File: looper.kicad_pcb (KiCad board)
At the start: 2 copper layers, 83 x 56.2 mm, 93 parts, among them CON1 BARREL_JACK, J1 JMP, J2 UART, J3 programming header, J4 Micro_SD_Card_Det, J5 electret mic, J6 line in, J7 line/~mic, J8 stereo_out, SW1 reset, SW2 RAM~FLASH, SW3 start, SW4 stop, SW5 Rotary_Encoder_Switch, U1 WM8778-units, U2 AP3211, U3 AZ1117C, U4 TC1185, U5 STM32F401RC, U6 lcd, U7 MAX4466, Y1 CSTLS4M00G53-B0

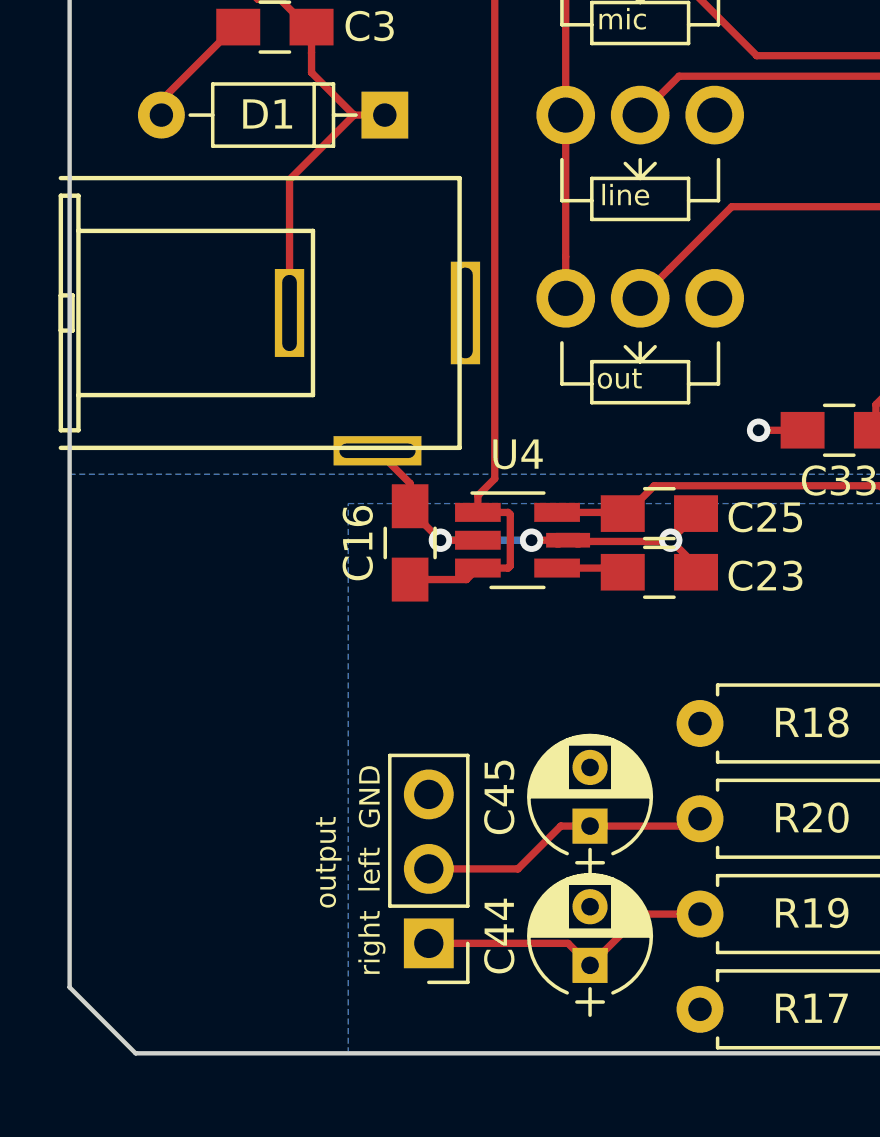
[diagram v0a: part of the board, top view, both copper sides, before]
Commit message: k: fix pcb
power connector trouble
wrong footprint for caps
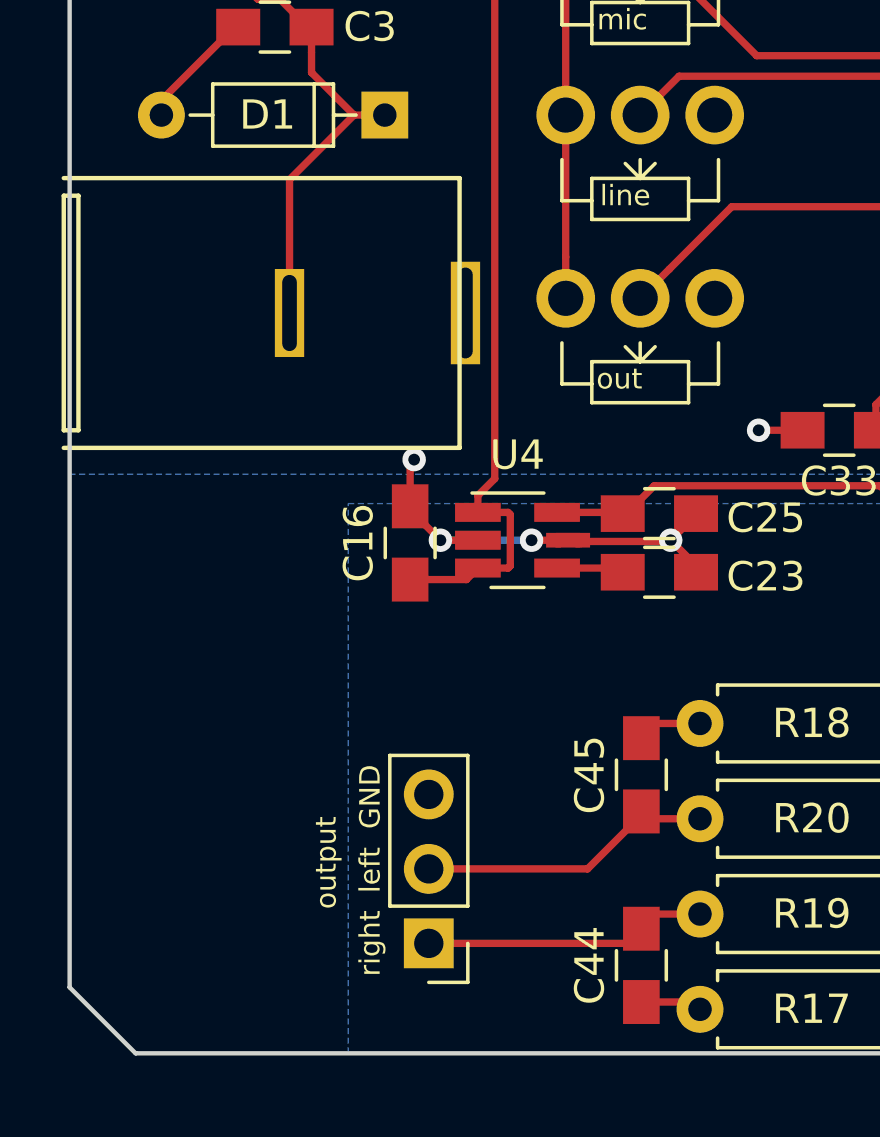
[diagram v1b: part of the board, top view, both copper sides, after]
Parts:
- C44, C45: footprint Capacitors_THT:CP_Radial_D4.0mm_P2.00mm -> Capacitors_SMD:C_0805_HandSoldering
- moved C45 2.47 mm to (68.8, 77.5)
- moved C44 1.75 mm to (68.8, 84.0), turned to 270 degrees
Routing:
- net AGND: track 21.7 -> 26.0 mm
- net GND: track 73.0 -> 72.3 mm, vias 25 -> 26
- net /Codec/voutl: track 9.96 -> 10.6 mm
- net /Codec/voutr: track 10.3 -> 9.66 mm

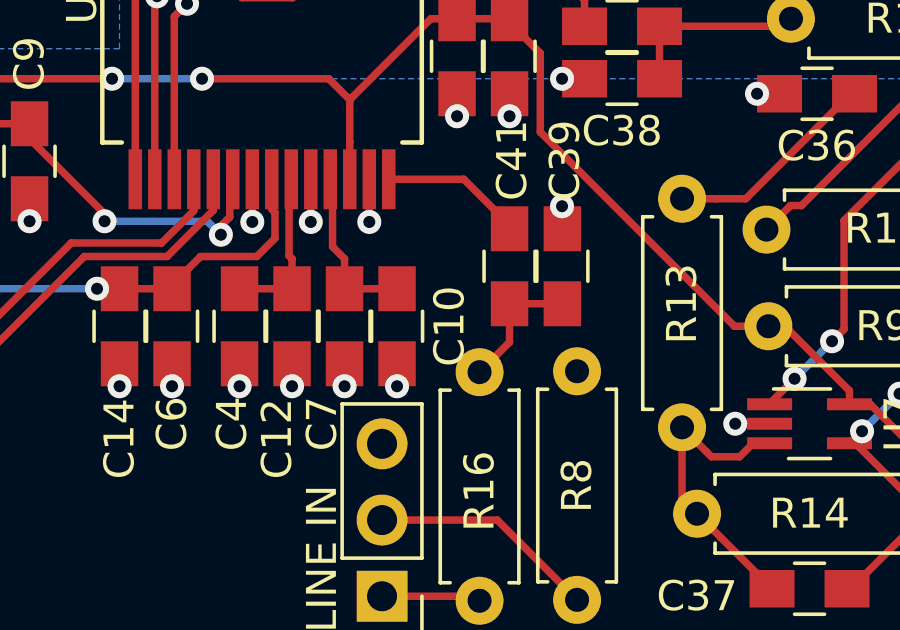
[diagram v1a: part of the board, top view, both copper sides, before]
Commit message: ksch: change component values to include the unit except for resistors add more info to some devices
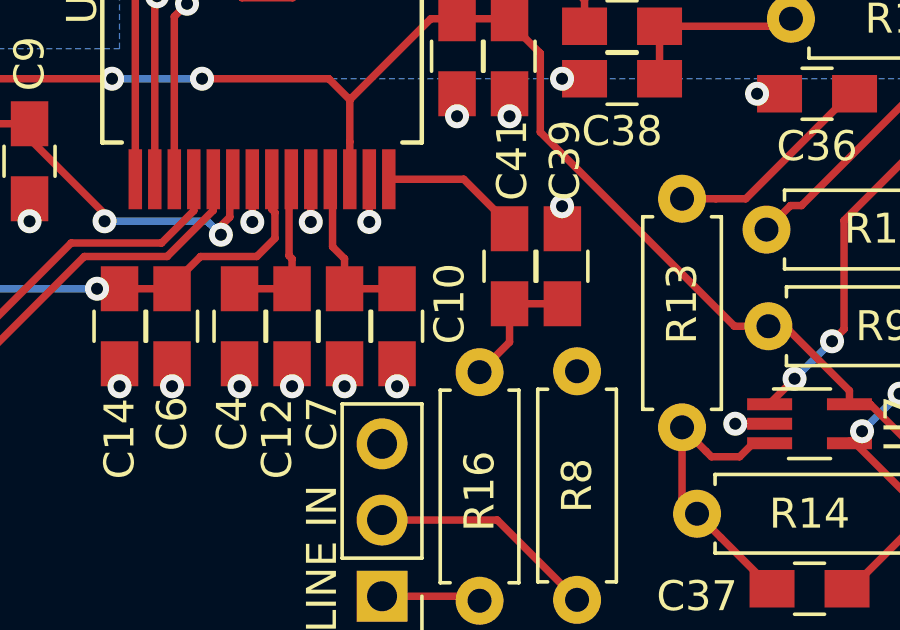
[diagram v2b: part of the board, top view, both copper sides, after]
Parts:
- C17, C33, C34: value 0.1u -> 100nF
- C19, C21, C26, C27, C28, C29: value 100n -> 100nF
- C2, C4, C5, C6, C7, C9: value 0.1uF -> 100nF
- C20, C36: value 1u -> 1uF
- C22, C30, C31: value 4.7u -> 4.7uF
- C32, C40, C41: value 10u -> 10uF
- C35: value 0.01u -> 10nF
- C37: value 100p -> 100pF
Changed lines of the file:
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@@
       (effects (font (size 1 1) (thickness 0.15)))
     )
-    (fp_text value 4.7u (at 0 1.75 270) (layer F.Fab)
+    (fp_text value 4.7uF (at 0 1.75 270) (layer F.Fab)
       (effects (font (size 1 1) (thickness 0.15)))
     )
@@
       (effects (font (size 1 1) (thickness 0.15)))
     )
-    (fp_text value 0.1u (at 0 1.75 90) (layer F.Fab)
+    (fp_text value 100nF (at 0 1.75 90) (layer F.Fab)
       (effects (font (size 1 1) (thickness 0.15)))
     )
@@
       (effects (font (size 1 1) (thickness 0.15)))
     )
-    (fp_text value 100n (at 0 1.75) (layer F.Fab)
+    (fp_text value 100nF (at 0 1.75) (layer F.Fab)
       (effects (font (size 1 1) (thickness 0.15)))
     )
@@
       (effects (font (size 1 1) (thickness 0.15)))
     )
-    (fp_text value 100n (at 0 1.75 90) (layer F.Fab)
+    (fp_text value 100nF (at 0 1.75 90) (layer F.Fab)
       (effects (font (size 1 1) (thickness 0.15)))
     )
@@
       (effects (font (size 1 1) (thickness 0.15)))
     )
-    (fp_text value 100n (at 0 1.75 180) (layer F.Fab)
+    (fp_text value 100nF (at 0 1.75 180) (layer F.Fab)
       (effects (font (size 1 1) (thickness 0.15)))
     )
@@
       (effects (font (size 1 1) (thickness 0.15)))
     )
-    (fp_text value 100n (at 0 1.75 270) (layer F.Fab)
+    (fp_text value 100nF (at 0 1.75 270) (layer F.Fab)
       (effects (font (size 1 1) (thickness 0.15)))
     )
@@
       (effects (font (size 1 1) (thickness 0.15)))
     )
-    (fp_text value 100n (at 0 1.75 270) (layer F.Fab)
+    (fp_text value 100nF (at 0 1.75 270) (layer F.Fab)
       (effects (font (size 1 1) (thickness 0.15)))
     )
@@
       (effects (font (size 1 1) (thickness 0.15)))
     )
-    (fp_text value 100n (at 0 1.75 90) (layer F.Fab)
+    (fp_text value 100nF (at 0 1.75 90) (layer F.Fab)
       (effects (font (size 1 1) (thickness 0.15)))
     )
@@
       (effects (font (size 1 1) (thickness 0.15)))
     )
-    (fp_text value 4.7u (at 0 1.75 90) (layer F.Fab)
+    (fp_text value 4.7uF (at 0 1.75 90) (layer F.Fab)
       (effects (font (size 1 1) (thickness 0.15)))
     )
@@
       (effects (font (size 1 1) (thickness 0.15)))
     )
-    (fp_text value 4.7u (at 0 1.75 90) (layer F.Fab)
+    (fp_text value 4.7uF (at 0 1.75 90) (layer F.Fab)
       (effects (font (size 1 1) (thickness 0.15)))
     )
@@
       (effects (font (size 1 1) (thickness 0.15)))
     )
-    (fp_text value 10u (at 0 1.75 90) (layer F.Fab)
+    (fp_text value 10uF (at 0 1.75 90) (layer F.Fab)
       (effects (font (size 1 1) (thickness 0.15)))
     )
@@
       (effects (font (size 1 1) (thickness 0.15)))
     )
-    (fp_text value 0.1u (at 0 1.75 180) (layer F.Fab)
+    (fp_text value 100nF (at 0 1.75 180) (layer F.Fab)
       (effects (font (size 1 1) (thickness 0.15)))
     )
@@
       (effects (font (size 1 1) (thickness 0.15)))
     )
-    (fp_text value 0.1u (at 0 1.75 90) (layer F.Fab)
+    (fp_text value 100nF (at 0 1.75 90) (layer F.Fab)
       (effects (font (size 1 1) (thickness 0.15)))
     )
@@
       (effects (font (size 1 1) (thickness 0.15)))
     )
-    (fp_text value 0.01u (at 0 1.75) (layer F.Fab)
+    (fp_text value 10nF (at 0 1.75) (layer F.Fab)
       (effects (font (size 1 1) (thickness 0.15)))
     )
@@
       (effects (font (size 1 1) (thickness 0.15)))
     )
-    (fp_text value 1u (at 0 1.75 180) (layer F.Fab)
+    (fp_text value 1uF (at 0 1.75 180) (layer F.Fab)
       (effects (font (size 1 1) (thickness 0.15)))
     )
@@
       (effects (font (size 1 1) (thickness 0.15)))
     )
-    (fp_text value 100p (at 0 1.75 180) (layer F.Fab)
+    (fp_text value 100pF (at 0 1.75 180) (layer F.Fab)
       (effects (font (size 1 1) (thickness 0.15)))
     )
@@
       (effects (font (size 1 1) (thickness 0.15)))
     )
-    (fp_text value 10u (at 0 0) (layer F.Fab)
+    (fp_text value 10uF (at 0 0) (layer F.Fab)
       (effects (font (size 1 1) (thickness 0.15)))
     )
@@
       (effects (font (size 1 1) (thickness 0.15)))
     )
-    (fp_text value 1u (at 0 0 90) (layer F.Fab)
+    (fp_text value 1uF (at 0 0 90) (layer F.Fab)
       (effects (font (size 1 1) (thickness 0.15)))
     )
@@
       (effects (font (size 1 1) (thickness 0.15)))
     )
-    (fp_text value 10u (at 0 1.75 270) (layer F.Fab)
+    (fp_text value 10uF (at 0 1.75 270) (layer F.Fab)
       (effects (font (size 1 1) (thickness 0.15)))
     )
@@
       (effects (font (size 1 1) (thickness 0.15)))
     )
-    (fp_text value 0.1uF (at 0 1.75 270) (layer F.Fab)
+    (fp_text value 100nF (at 0 1.75 270) (layer F.Fab)
       (effects (font (size 1 1) (thickness 0.15)))
     )
@@
       (effects (font (size 1 1) (thickness 0.15)))
     )
-    (fp_text value 0.1uF (at 0 1.75 270) (layer F.Fab)
+    (fp_text value 100nF (at 0 1.75 270) (layer F.Fab)
       (effects (font (size 1 1) (thickness 0.15)))
     )
@@
       (effects (font (size 1 1) (thickness 0.15)))
     )
-    (fp_text value 0.1uF (at 0 1.75 270) (layer F.Fab)
+    (fp_text value 100nF (at 0 1.75 270) (layer F.Fab)
       (effects (font (size 1 1) (thickness 0.15)))
     )
@@
       (effects (font (size 1 1) (thickness 0.15)))
     )
-    (fp_text value 0.1uF (at 0 1.75 270) (layer F.Fab)
+    (fp_text value 100nF (at 0 1.75 270) (layer F.Fab)
       (effects (font (size 1 1) (thickness 0.15)))
     )
@@
       (effects (font (size 1 1) (thickness 0.15)))
     )
-    (fp_text value 0.1uF (at 0 1.75 270) (layer F.Fab)
+    (fp_text value 100nF (at 0 1.75 270) (layer F.Fab)
       (effects (font (size 1 1) (thickness 0.15)))
     )
@@
     (tags "capacitor 0805")
     (attr smd)
-    (fp_text reference C10 (at 0 -1.75 270) (layer F.SilkS)
+    (fp_text reference C10 (at -0.75 -1.75 270) (layer F.SilkS)
       (effects (font (size 1 1) (thickness 0.15)))
     )
@@
       (effects (font (size 1 1) (thickness 0.15)))
     )
-    (fp_text user %R (at 0 -1.75 270) (layer F.Fab)
+    (fp_text user %R (at -0.75 -1.75 270) (layer F.Fab)
       (effects (font (size 1 1) (thickness 0.15)))
     )
@@
       (effects (font (size 1 1) (thickness 0.15)))
     )
-    (fp_text value 0.1uF (at 0 1.75) (layer F.Fab)
-      (effects (font (size 1 1) (thickness 0.15)))
-    )
+    (fp_text value 100nF (at 0 1.75) (layer F.Fab)
+      (effects (font (size 1 1) (thickness 0.15)))
+    )

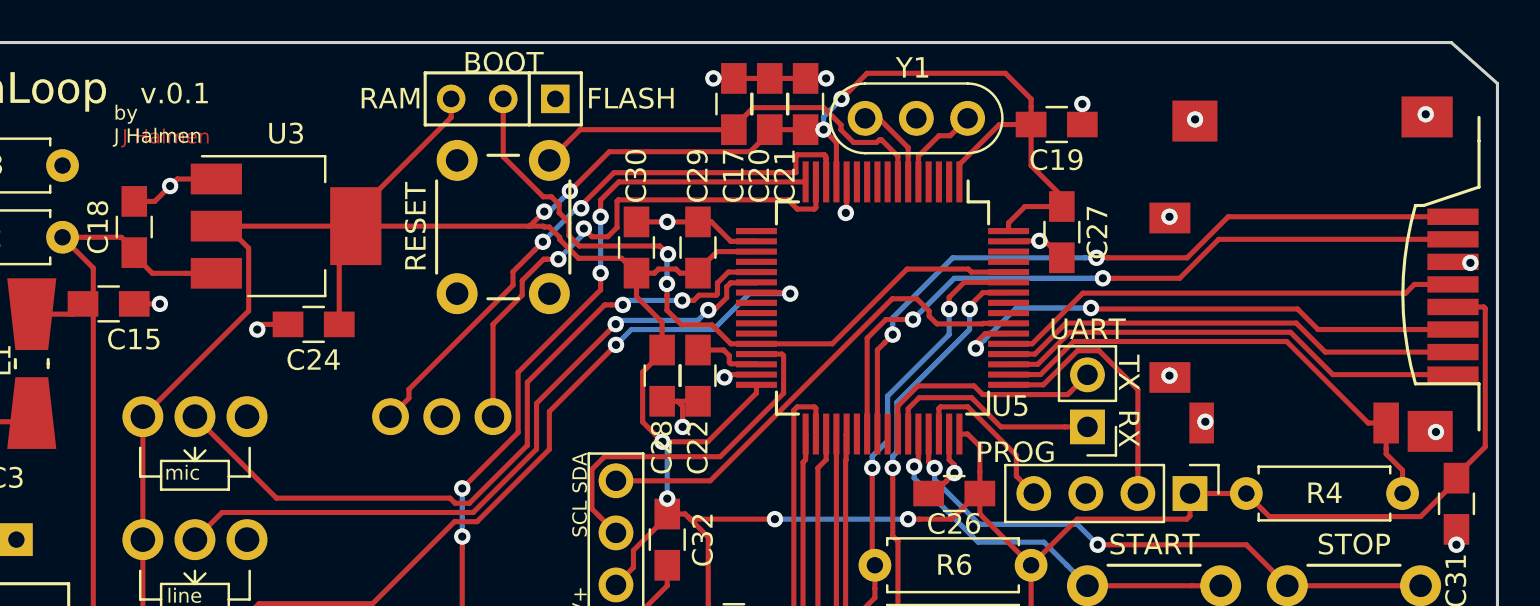
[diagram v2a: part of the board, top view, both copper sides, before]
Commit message: pcb: use fixed sd footprints, reroute
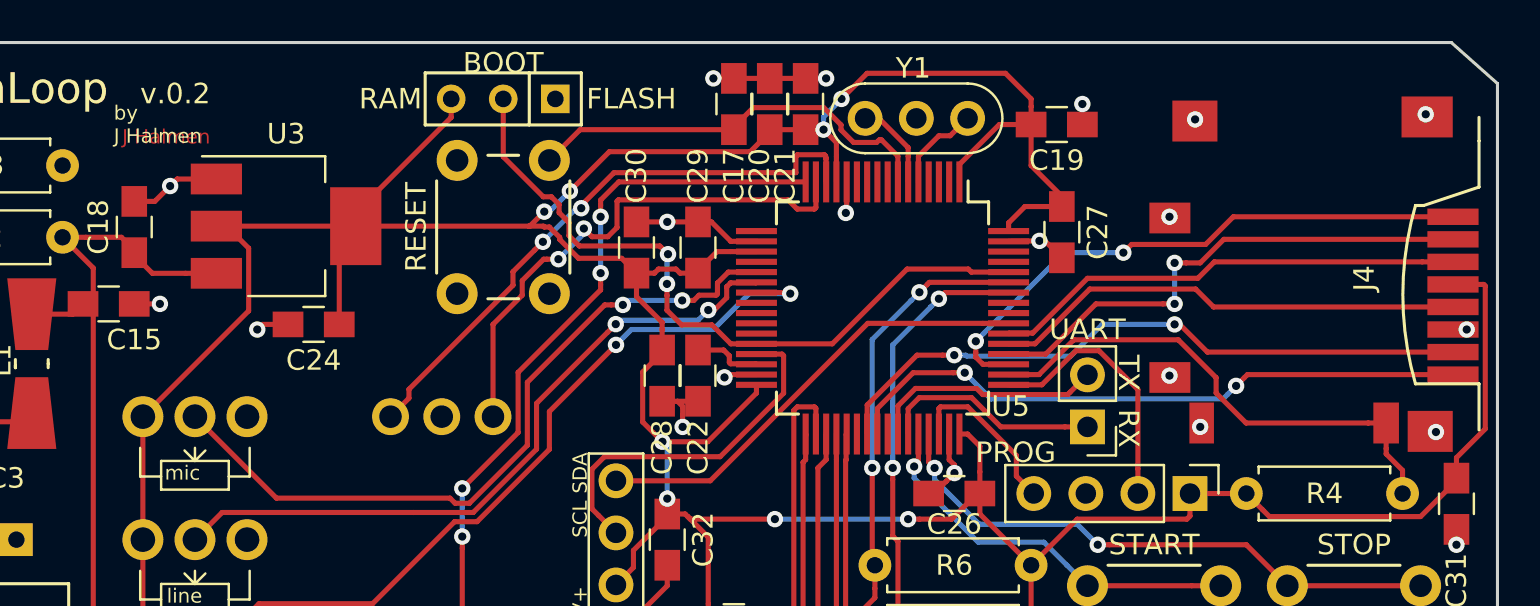
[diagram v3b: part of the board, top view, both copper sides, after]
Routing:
- net /controller/SDIO_D2: track 23.2 -> 28.3 mm, vias 0 -> 2
- net /controller/SDIO_D1: track 35.4 -> 31.1 mm
- net /controller/SDIO_CMD: track 26.6 -> 23.4 mm, vias 2 -> 0
- net /controller/SDIO_D0: track 35.3 -> 32.2 mm
- net /controller/SDIO_D3: track 22.9 -> 25.2 mm, vias 0 -> 2
- net 3.3V: track 217.6 -> 218.8 mm
- net /controller/DISP_SDA: track 23.5 -> 22.3 mm
- net /controller/I2C1_SCL: track 35.6 -> 36.7 mm
- net /controller/I2C1_SDA: track 36.9 -> 37.9 mm
- net /controller/SDdetect: track 24.5 -> 25.0 mm
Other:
- board text added: "v.0.2"
- board text removed: "v.0.1"

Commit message: migrate to kicad v5
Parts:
- C35: value 10nF -> 10nF C0G/NP0
- C38, C39, C44, C45: value 4.7nF -> 4.7nF C0G/NP0
- C40, C41, C42, C43: value 10uF -> 10uF C0G/NP0
- U2: value AP3211 -> AP3211KTR
- U3: value AZ1117C -> AZ1117CH-3.3
- U4: value TC1185 -> TC1185-5.0
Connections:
- R16 pad 1: Net-(J6-Pad1) -> Net-(J6-PadT)
- R8 pad 2: Net-(J6-Pad2) -> Net-(J6-PadTN)
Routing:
- net Net-(J6-PadTN): track 0.00 -> 7.60 mm
- net Net-(J6-Pad2): track 7.60 -> 0.00 mm
- net Net-(J6-PadT): track 0.00 -> 3.31 mm
- net Net-(J6-Pad1): track 3.31 -> 0.00 mm
